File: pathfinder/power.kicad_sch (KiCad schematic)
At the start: 16 parts, among them IC5 ST730M33R, U2 LP2985-1.8

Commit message: Start components layout
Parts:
- C10, C11, C15, C16, C17, C9: footprint Capacitor_SMD:C_0603_1608Metric_Pad1.08x0.95mm_HandSolder -> Capacitor_SMD:C_0402_1005Metric_Pad0.74x0.62mm_HandSolder
- D4, D5, D8: footprint Diode_SMD:D_0603_1608Metric_Pad1.05x0.95mm_HandSolder -> Diode_SMD:D_0402_1005Metric_Pad0.77x0.64mm_HandSolder
- R5, R7, R8: footprint Resistor_SMD:R_0603_1608Metric_Pad0.98x0.95mm_HandSolder -> Resistor_SMD:R_0402_1005Metric_Pad0.72x0.64mm_HandSolder
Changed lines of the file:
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@@
 			)
 		)
-		(property "Footprint" "Diode_SMD:D_0603_1608Metric_Pad1.05x0.95mm_HandSolder"
+		(property "Footprint" "Diode_SMD:D_0402_1005Metric_Pad0.77x0.64mm_HandSolder"
 			(at 128.27 102.87 90)
 			(effects
@@
 			)
 		)
-		(property "Footprint" "Capacitor_SMD:C_0603_1608Metric_Pad1.08x0.95mm_HandSolder"
+		(property "Footprint" "Capacitor_SMD:C_0402_1005Metric_Pad0.74x0.62mm_HandSolder"
 			(at 138.43 130.81 0)
 			(effects
@@
 			)
 		)
-		(property "Footprint" "Diode_SMD:D_0603_1608Metric_Pad1.05x0.95mm_HandSolder"
+		(property "Footprint" "Diode_SMD:D_0402_1005Metric_Pad0.77x0.64mm_HandSolder"
 			(at 180.34 102.87 90)
 			(effects
@@
 			)
 		)
-		(property "Footprint" "Capacitor_SMD:C_0603_1608Metric_Pad1.08x0.95mm_HandSolder"
+		(property "Footprint" "Capacitor_SMD:C_0402_1005Metric_Pad0.74x0.62mm_HandSolder"
 			(at 118.11 82.55 0)
 			(effects
@@
 			)
 		)
-		(property "Footprint" "Capacitor_SMD:C_0603_1608Metric_Pad1.08x0.95mm_HandSolder"
+		(property "Footprint" "Capacitor_SMD:C_0402_1005Metric_Pad0.74x0.62mm_HandSolder"
 			(at 165.1 130.81 0)
 			(effects
@@
 			)
 		)
-		(property "Footprint" "Capacitor_SMD:C_0603_1608Metric_Pad1.08x0.95mm_HandSolder"
+		(property "Footprint" "Capacitor_SMD:C_0402_1005Metric_Pad0.74x0.62mm_HandSolder"
 			(at 170.18 100.33 0)
 			(effects
@@
 			)
 		)
-		(property "Footprint" "Resistor_SMD:R_0603_1608Metric_Pad0.98x0.95mm_HandSolder"
+		(property "Footprint" "Resistor_SMD:R_0402_1005Metric_Pad0.72x0.64mm_HandSolder"
 			(at 128.27 76.2 0)
 			(effects
@@
 			)
 		)
-		(property "Footprint" "Resistor_SMD:R_0603_1608Metric_Pad0.98x0.95mm_HandSolder"
+		(property "Footprint" "Resistor_SMD:R_0402_1005Metric_Pad0.72x0.64mm_HandSolder"
 			(at 180.34 96.52 0)
 			(effects
@@
 			)
 		)
-		(property "Footprint" "Capacitor_SMD:C_0603_1608Metric_Pad1.08x0.95mm_HandSolder"
+		(property "Footprint" "Capacitor_SMD:C_0402_1005Metric_Pad0.74x0.62mm_HandSolder"
 			(at 173.99 130.81 0)
 			(effects
@@
 			)
 		)
-		(property "Footprint" "Capacitor_SMD:C_0603_1608Metric_Pad1.08x0.95mm_HandSolder"
+		(property "Footprint" "Capacitor_SMD:C_0402_1005Metric_Pad0.74x0.62mm_HandSolder"
 			(at 118.11 95.25 0)
 			(effects
@@
 			)
 		)
-		(property "Footprint" "Diode_SMD:D_0603_1608Metric_Pad1.05x0.95mm_HandSolder"
+		(property "Footprint" "Diode_SMD:D_0402_1005Metric_Pad0.77x0.64mm_HandSolder"
 			(at 128.27 69.85 90)
 			(effects
@@
 			)
 		)
-		(property "Footprint" "Resistor_SMD:R_0603_1608Metric_Pad0.98x0.95mm_HandSolder"
+		(property "Footprint" "Resistor_SMD:R_0402_1005Metric_Pad0.72x0.64mm_HandSolder"
 			(at 128.27 96.52 0)
 			(effects

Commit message: Board finished
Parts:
- removed D4: Green, Diode_SMD:D_0402_1005Metric_Pad0.77x0.64mm_HandSolder, symbol Device:LED_Small
- removed R5: 420, Resistor_SMD:R_0402_1005Metric_Pad0.72x0.64mm_HandSolder, symbol Device:R_Small
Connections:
- net PWR: now reaches C10.1, C11.1, C15.1, D3.1 (K), D7.1 (K), IC5.3 (VIN), IC5.5 (EN), R7.2, U2.1 (VIN), U2.3 (ON/~{OFF})
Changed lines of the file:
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@@
 	(paper "A4")
-	(junction
-		(at 128.27 92.71)
-		(diameter 0)
-		(color 0 0 0 0)
-	)
 	(junction
 		(at 118.11 80.01)
@@
 	)
 	(junction
+		(at 138.43 80.01)
+		(diameter 0)
+		(color 0 0 0 0)
+	)
+	(junction
 		(at 173.99 124.46)
 		(diameter 0)
@@
 	(wire
 		(pts
-			(xy 128.27 105.41) (xy 128.27 106.68)
-		)
-		(stroke
-			(width 0)
-			(type default)
-		)
-	)
-	(wire
-		(pts
 			(xy 180.34 92.71) (xy 170.18 92.71)
 		)
@@
 	(wire
 		(pts
-			(xy 118.11 92.71) (xy 128.27 92.71)
-		)
-		(stroke
-			(width 0)
-			(type default)
-		)
-	)
-	(wire
-		(pts
 			(xy 138.43 124.46) (xy 138.43 96.52)
 		)
@@
 	(wire
 		(pts
-			(xy 128.27 93.98) (xy 128.27 92.71)
-		)
-		(stroke
-			(width 0)
-			(type default)
-		)
-	)
-	(wire
-		(pts
 			(xy 138.43 124.46) (xy 138.43 127)
 		)
@@
 	(wire
 		(pts
-			(xy 128.27 99.06) (xy 128.27 100.33)
-		)
-		(stroke
-			(width 0)
-			(type default)
-		)
-	)
-	(wire
-		(pts
 			(xy 165.1 127) (xy 163.83 127)
 		)
@@
 	(wire
 		(pts
-			(xy 128.27 92.71) (xy 138.43 92.71)
+			(xy 118.11 92.71) (xy 138.43 92.71)
 		)
 		(stroke
@@
 		)
 	)
-	(symbol
-		(lib_id "Device:LED_Small")
-		(at 128.27 102.87 90)
-		(unit 1)
-		(exclude_from_sim no)
-		(in_bom yes)
-		(on_board yes)
-		(dnp no)
+	(label "PWR"
+		(at 138.43 80.01 180)
 		(fields_autoplaced yes)
-		(property "Reference" "D4"
-			(at 130.81 101.5364 90)
-			(effects
-				(font
-					(size 1.27 1.27)
-				)
-				(justify right)
-			)
-		)
-		(property "Value" "Green"
-			(at 130.81 104.0764 90)
-			(effects
-				(font
-					(size 1.27 1.27)
-				)
-				(justify right)
-			)
-		)
-		(property "Footprint" "Diode_SMD:D_0402_1005Metric_Pad0.77x0.64mm_HandSolder"
-			(at 128.27 102.87 90)
-			(effects
-				(font
-					(size 1.27 1.27)
-				)
-				(hide yes)
-			)
-		)
-		(property "Datasheet" "~"
-			(at 128.27 102.87 90)
-			(effects
-				(font
-					(size 1.27 1.27)
-				)
-				(hide yes)
-			)
-		)
-		(property "Description" "Light emitting diode, small symbol"
-			(at 128.27 102.87 0)
-			(effects
-				(font
-					(size 1.27 1.27)
-				)
-				(hide yes)
-			)
-		)
-		(pin "2"
-		)
-		(pin "1"
-		)
-		(instances
-			(project "sensor_fuser"
-				(path "/07668456-3e33-43d1-9c6d-92adc10437c4/b3b8fb8f-5444-4bb9-8b28-7dde226aad59"
-					(reference "D4")
-					(unit 1)
-				)
-			)
+		(effects
+			(font
+				(size 1.27 1.27)
+			)
+			(justify right bottom)
 		)
 	)
@@
 	)
 	(symbol
-		(lib_id "power:GND")
-		(at 128.27 106.68 0)
-		(unit 1)
-		(exclude_from_sim no)
-		(in_bom yes)
-		(on_board yes)
-		(dnp no)
-		(property "Reference" "#PWR016"
-			(at 128.27 113.03 0)
-			(effects
-				(font
-					(size 1.27 1.27)
-				)
-				(hide yes)
-			)
-		)
-		(property "Value" "GND"
-			(at 128.27 110.49 0)
-			(effects
-				(font
-					(size 1.27 1.27)
-				)
-			)
-		)
-		(property "Footprint" ""
-			(at 128.27 106.68 0)
-			(effects
-				(font
-					(size 1.27 1.27)
-				)
-				(hide yes)
-			)
-		)
-		(property "Datasheet" ""
-			(at 128.27 106.68 0)
-			(effects
-				(font
-					(size 1.27 1.27)
-				)
-				(hide yes)
-			)
-		)
-		(property "Description" "Power symbol creates a global label with name \"GND\" , ground"
-			(at 128.27 106.68 0)
-			(effects
-				(font
-					(size 1.27 1.27)
-				)
-				(hide yes)
-			)
-		)
-		(pin "1"
-		)
-		(instances
-			(project "sensor_fuser"
-				(path "/07668456-3e33-43d1-9c6d-92adc10437c4/b3b8fb8f-5444-4bb9-8b28-7dde226aad59"
-					(reference "#PWR016")
-					(unit 1)
-				)
-			)
-		)
-	)
-	(symbol
 		(lib_id "Device:LED_Small")
 		(at 180.34 102.87 90)
@@
 	)
 	(symbol
+		(lib_id "power:PWR_FLAG")
+		(at 138.43 80.01 270)
+		(unit 1)
+		(exclude_from_sim no)
+		(in_bom yes)
+		(on_board yes)
+		(dnp no)
+		(fields_autoplaced yes)
+		(property "Reference" "#FLG01"
+			(at 140.335 80.01 0)
+			(effects
+				(font
+					(size 1.27 1.27)
+				)
+				(hide yes)
+			)
+		)
+		(property "Value" "PWR_FLAG"
+			(at 142.24 80.0099 90)
+			(effects
+				(font
+					(size 1.27 1.27)
+				)
+				(justify left)
+			)
+		)
+		(property "Footprint" ""
+			(at 138.43 80.01 0)
+			(effects
+				(font
+					(size 1.27 1.27)
+				)
+				(hide yes)
+			)
+		)
+		(property "Datasheet" "~"
+			(at 138.43 80.01 0)
+			(effects
+				(font
+					(size 1.27 1.27)
+				)
+				(hide yes)
+			)
+		)
+		(property "Description" "Special symbol for telling ERC where power comes from"
+			(at 138.43 80.01 0)
+			(effects
+				(font
+					(size 1.27 1.27)
+				)
+				(hide yes)
+			)
+		)
+		(pin "1"
+		)
+		(instances
+			(project ""
+				(path "/07668456-3e33-43d1-9c6d-92adc10437c4/b3b8fb8f-5444-4bb9-8b28-7dde226aad59"
+					(reference "#FLG01")
+					(unit 1)
+				)
+			)
+		)
+	)
+	(symbol
 		(lib_id "power:+3V3")
 		(at 170.18 82.55 0)
@@
 					(unit 1)
 				)
-			)
-		)
-	)
-	(symbol
-		(lib_id "Device:R_Small")
-		(at 128.27 96.52 180)
-		(unit 1)
-		(exclude_from_sim no)
-		(in_bom yes)
-		(on_board yes)
-		(dnp no)
-		(fields_autoplaced yes)
-		(property "Reference" "R5"
-			(at 130.81 95.2499 0)
-			(effects
-				(font
-					(size 1.27 1.27)
-				)
-				(justify right)
-			)
-		)
-		(property "Value" "420"
-			(at 130.81 97.7899 0)
-			(effects
-				(font
-					(size 1.27 1.27)
-				)
-				(justify right)
-			)
-		)
-		(property "Footprint" "Resistor_SMD:R_0402_1005Metric_Pad0.72x0.64mm_HandSolder"
-			(at 128.27 96.52 0)
-			(effects
-				(font
-					(size 1.27 1.27)
-				)
-				(hide yes)
-			)
-		)
-		(property "Datasheet" "~"
-			(at 128.27 96.52 0)
-			(effects
-				(font
-					(size 1.27 1.27)
-				)
-				(hide yes)
-			)
-		)
-		(property "Description" "Resistor, small symbol"
-			(at 128.27 96.52 0)
-			(effects
-				(font
-					(size 1.27 1.27)
-				)
-				(hide yes)
-			)
-		)
-		(pin "1"
-		)
-		(pin "2"
-		)
-		(instances
-			(project "sensor_fuser"
-				(path "/07668456-3e33-43d1-9c6d-92adc10437c4/b3b8fb8f-5444-4bb9-8b28-7dde226aad59"
-					(reference "R5")
-					(unit 1)
-				)

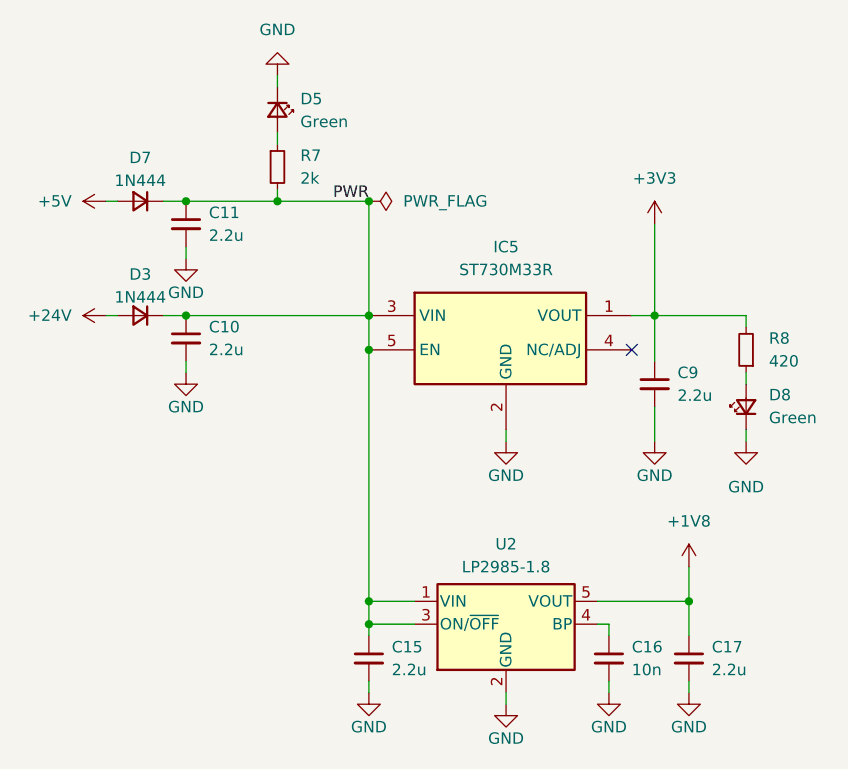
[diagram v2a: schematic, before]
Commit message: change 1v8 ldo power supply
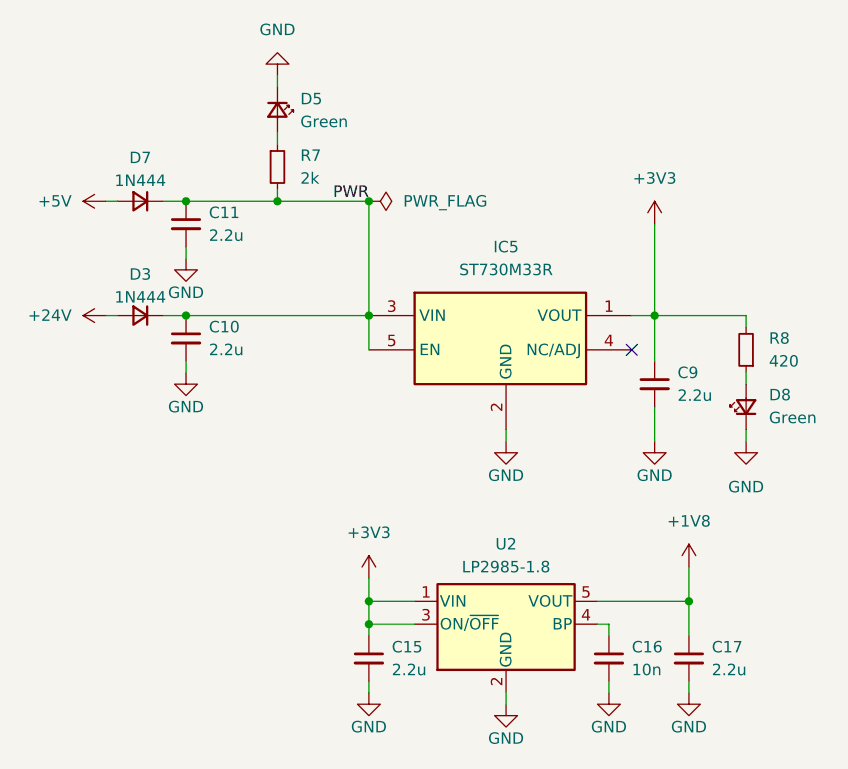
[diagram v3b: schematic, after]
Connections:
- net +3V3: now also C15.1, U2.1 (VIN), U2.3 (ON/~{OFF})
- net PWR: no longer C15.1, U2.1 (VIN), U2.3 (ON/~{OFF})
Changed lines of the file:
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@@
 	(paper "A4")
+	(junction
+		(at 138.43 124.46)
+		(diameter 0)
+		(color 0 0 0 0)
+	)
 	(junction
 		(at 118.11 80.01)
@@
 	)
 	(junction
-		(at 138.43 124.46)
-		(diameter 0)
-		(color 0 0 0 0)
-	)
-	(junction
 		(at 138.43 127)
-		(diameter 0)
-		(color 0 0 0 0)
-	)
-	(junction
-		(at 138.43 96.52)
 		(diameter 0)
 		(color 0 0 0 0)
@@
 	(wire
 		(pts
-			(xy 138.43 124.46) (xy 138.43 96.52)
-		)
-		(stroke
-			(width 0)
-			(type default)
-		)
-	)
-	(wire
-		(pts
 			(xy 138.43 124.46) (xy 138.43 127)
 		)
@@
 		(pts
 			(xy 115.57 80.01) (xy 118.11 80.01)
+		)
+		(stroke
+			(width 0)
+			(type default)
+		)
+	)
+	(wire
+		(pts
+			(xy 138.43 121.92) (xy 138.43 124.46)
 		)
 		(stroke
@@
 					(unit 1)
 				)
+			)
+		)
+	)
+	(symbol
+		(lib_id "power:+3V3")
+		(at 138.43 121.92 0)
+		(unit 1)
+		(exclude_from_sim no)
+		(in_bom yes)
+		(on_board yes)
+		(dnp no)
+		(fields_autoplaced yes)
+		(property "Reference" "#PWR030"
+			(at 138.43 125.73 0)
+			(effects
+				(font
+					(size 1.27 1.27)
+				)
+				(hide yes)
+			)
+		)
+		(property "Value" "+3V3"
+			(at 138.43 116.84 0)
+			(effects
+				(font
+					(size 1.27 1.27)
+				)
+			)
+		)
+		(property "Footprint" ""
+			(at 138.43 121.92 0)
+			(effects
+				(font
+					(size 1.27 1.27)
+				)
+				(hide yes)
+			)
+		)
+		(property "Datasheet" ""
+			(at 138.43 121.92 0)
+			(effects
+				(font
+					(size 1.27 1.27)
+				)
+				(hide yes)
+			)
+		)
+		(property "Description" "Power symbol creates a global label with name \"+3V3\""
+			(at 138.43 121.92 0)
+			(effects
+				(font
+					(size 1.27 1.27)
+				)
+				(hide yes)
+			)
+		)
+		(pin "1"
+		)
+		(instances
+			(project "pathfinder"
+				(path "/07668456-3e33-43d1-9c6d-92adc10437c4/b3b8fb8f-5444-4bb9-8b28-7dde226aad59"
+					(reference "#PWR030")
+					(unit 1)
+				)
